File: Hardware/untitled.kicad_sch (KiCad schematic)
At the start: 15 parts, among them IC1 LM74502HDDFR, J3 CarLVPowerConnector, Q12 PSMN8R5-40MSDX

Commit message: revB updates
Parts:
- removed D10: SMBJ30CA, DIOM5436X244N, symbol TVS Diode:SMBJ30CA
- removed D12: CDBC560-G, Schlotty:DIOM7959X262N, symbol Schott:CDBC560-G
- removed LVPRW_TP2: TestPoint, TestPoint:TestPoint_Pad_1.0x1.0mm, symbol Connector:TestPoint
- removed Q12: PSMN8R5-40MSDX, UTSVT_Power:PSMN8R5-40MSDX, symbol utsvt_power:PSMN8R5-40MSDX
- removed R28: 200k, Resistor_SMD:R_0603_1608Metric, symbol Device:R_US
- removed R51: 9.1k, Resistor_SMD:R_0603_1608Metric, symbol Device:R_US
- added C37: 10u, Capacitor_SMD:C_0805_2012Metric_Pad1.18x1.45mm_HandSolder, symbol Device:C
- added C38: 0.1u, Capacitor_SMD:C_0603_1608Metric_Pad1.08x0.95mm_HandSolder, symbol Device:C
- added C5: 1u, Capacitor_SMD:C_0603_1608Metric_Pad1.08x0.95mm_HandSolder, symbol Device:C
- added D10: SMAF4758A, UTSVT_Passives:SODFL5026X125N, symbol Device:D_Zener
- added LVGND_TP1: TestPoint, TestPoint:TestPoint_Pad_2.0x2.0mm, symbol Connector:TestPoint
- added LVPWR1: LED, LED_SMD:LED_0603_1608Metric_Pad1.05x0.95mm_HandSolder, symbol Device:LED
- added Q12, Q2: NVMFWS1D7N04XMT1G, UTSVT_Power:NVMFWS3D0P04M8LT1G, symbol UTSVT_Power:NVMFWS1D7N04XMT1G
- added R14: 200k, Resistor_SMD:R_0603_1608Metric_Pad0.98x0.95mm_HandSolder, symbol Device:R_US
- added R18: 9k, Resistor_SMD:R_0603_1608Metric_Pad0.98x0.95mm_HandSolder, symbol Device:R_US
- added R83: 4.3k, Resistor_SMD:R_0603_1608Metric_Pad0.98x0.95mm_HandSolder, symbol Device:R_US
- 24V_TP1: footprint TestPoint:TestPoint_Pad_1.0x1.0mm -> TestPoint:TestPoint_Pad_2.0x2.0mm
- C20: value 1u -> 220n; footprint Capacitor_SMD:C_0603_1608Metric -> Capacitor_SMD:C_0603_1608Metric_Pad1.08x0.95mm_HandSolder; Manufactuerer TAIYO YUDEN -> (none); Mouser Part Number (none) -> 963-MSASU168SB7224KT; P/N MLASU168SB5105KTNA01 -> MSASU168SB7224KTNB25
- C21: footprint Capacitor_SMD:C_0805_2012Metric -> Capacitor_SMD:C_0805_2012Metric_Pad1.18x1.45mm_HandSolder; Manufactuerer Murata Electronics -> (none); Mouser Part Number (none) -> 81-GRM21BR61H106KE3K
- C3: value 220n -> 1u; footprint Capacitor_SMD:C_0603_1608Metric -> Capacitor_SMD:C_0603_1608Metric_Pad1.08x0.95mm_HandSolder; Manufactuerer TAIYO YUDEN -> (none); Mouser Part Number (none) -> 963-UMK107BJ105KA-T; P/N MSASU168SB7224KTNB25 -> UMK107BJ105KA-T
- C4: Manufactuerer TAIYO YUDEN -> (none); Mouser Part Number (none) -> 963-HMK107B7104KA-T; P/N MLASH168SB7104KTNA01 -> HMK107B7104KA-T
- IC1: Manufactuerer Texas Instruments -> (none); Manufacturer_Part_Number (none) -> LM74502HDDFR
- J3: Manufactuerer Molex -> (none); Mouser Part Number (none) -> 538-105309-1102; P/N 105309-1102 -> 105309-1102
- R28: renamed from R18; footprint Resistor_SMD:R_0603_1608Metric -> Resistor_SMD:R_0603_1608Metric_Pad0.98x0.95mm_HandSolder; Manufactuerer Vishay -> (none); Mouser Part Number (none) -> 71-CRCW060310K0FKEI; P/N CRCW060310K0FKEI -> CRCW060310K0FKEI
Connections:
- net +24V: now also C37.1, C38.1, Q12.5 (D), Q12.6 (D), Q12.7 (D), Q12.8 (D), Q12.9 (D), R83.1; no longer IC1.8 (SRC)
- net GND: now also C3.1, C4.2, C37.2, C38.2, C5.2, D10.2 (A), LVGND_TP1.1, LVPWR1.1 (K), R18.2; no longer C20.1, C4.1
- net LV+: now also C4.1, R28.1, C5.1, Q2.5 (D), Q2.6 (D), Q2.7 (D), Q2.8 (D), Q2.9 (D), R14.1
- net RPP_EN: now also C20.1, C3.2, D10.1 (K); no longer C20.2, C3.1
- net at IC1.4 (VCAP): now also C20.2; no longer C3.2
- net at IC1.6 (GATE): now also Q12.4 (G), Q2.4 (G)
- net at IC1.7 (OV): now also R14.2, R18.1
- new net: IC1.8 (SRC), Q12.1 (S), Q12.2 (S), Q12.3 (S), Q2.1 (S), Q2.2 (S), Q2.3 (S)
- new net: LVPWR1.2 (A), R83.2
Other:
- note added: "24V Input Bypass Cap"
- note added: "LV PWR indicator LED"
- note added: "RPP Protection"
- note removed: "RPP Protection, Direct from VCU (circa 09/09/2025)"
- moved on the sheet: 24V_TP1, 3.3V_In1, IC1, R28

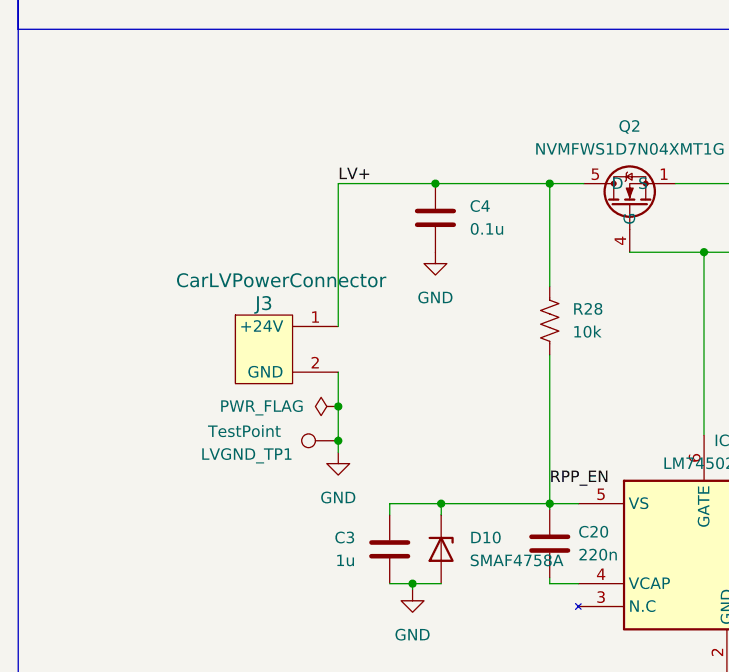
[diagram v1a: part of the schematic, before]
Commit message: Schematic polishes, layout WIP
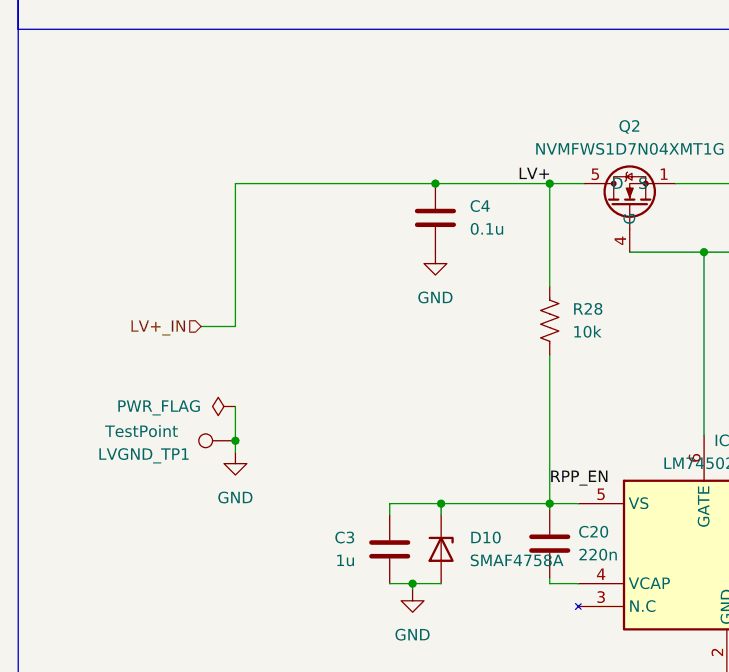
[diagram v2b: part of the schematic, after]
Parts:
- removed J3: CarLVPowerConnector, UTSVT_Connectors:Molex_Nano-Fit_105309-xx02_1x02_P2.50mm_Vertical, symbol UTSVT_Connectors:CarLVPowerConnector
- C20, C3, C38, C4, C5: footprint Capacitor_SMD:C_0603_1608Metric_Pad1.08x0.95mm_HandSolder -> Capacitor_SMD:C_0603_1608Metric
- C21, C37: footprint Capacitor_SMD:C_0805_2012Metric_Pad1.18x1.45mm_HandSolder -> Capacitor_SMD:C_0805_2012Metric
- LVPWR1: footprint LED_SMD:LED_0603_1608Metric_Pad1.05x0.95mm_HandSolder -> LED_SMD:LED_0603_1608Metric
- R14, R18, R28, R83: footprint Resistor_SMD:R_0603_1608Metric_Pad0.98x0.95mm_HandSolder -> Resistor_SMD:R_0603_1608Metric
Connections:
- net LV+ renamed LV+_IN
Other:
- moved on the sheet: LVGND_TP1
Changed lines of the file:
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@@
 	)
 	(junction
-		(at 73.025 53.975)
-		(diameter 0)
-		(color 0 0 0 0)
-	)
-	(junction
 		(at 70.485 98.425)
 		(diameter 0)
@@
 	)
 	(junction
-		(at 62.23 82.55)
+		(at 50.8 82.55)
 		(diameter 0)
 		(color 0 0 0 0)
 	)
 	(junction
-		(at 62.23 78.74)
+		(at 73.025 53.975)
 		(diameter 0)
 		(color 0 0 0 0)
@@
 	(wire
 		(pts
-			(xy 62.23 53.975) (xy 62.23 69.85)
+			(xy 46.99 69.85) (xy 50.8 69.85)
+		)
+		(stroke
+			(width 0)
+			(type default)
+		)
+	)
+	(wire
+		(pts
+			(xy 50.8 53.975) (xy 50.8 69.85)
 		)
 		(stroke
@@
 	(wire
 		(pts
-			(xy 62.23 78.74) (xy 62.23 82.55)
+			(xy 50.8 78.74) (xy 50.8 82.55)
 		)
 		(stroke
@@
 	(wire
 		(pts
-			(xy 62.23 83.82) (xy 62.23 82.55)
+			(xy 50.8 83.82) (xy 50.8 82.55)
 		)
 		(stroke
@@
 	(wire
 		(pts
-			(xy 231.14 69.85) (xy 231.14 78.74)
+			(xy 50.8 53.975) (xy 73.025 53.975)
 		)
 		(stroke
@@
 	(wire
 		(pts
-			(xy 231.14 54.61) (xy 231.14 62.23)
-		)
-		(stroke
-			(width 0)
-			(type default)
-		)
-	)
-	(wire
-		(pts
-			(xy 85.725 89.535) (xy 85.725 90.17)
+			(xy 231.14 69.85) (xy 231.14 78.74)
 		)
 		(stroke
@@
 	(wire
 		(pts
-			(xy 218.44 54.61) (xy 218.44 62.23)
+			(xy 231.14 54.61) (xy 231.14 62.23)
 		)
 		(stroke
@@
 	(wire
 		(pts
-			(xy 140.335 53.975) (xy 140.335 56.515)
+			(xy 85.725 89.535) (xy 85.725 90.17)
 		)
 		(stroke
@@
 	(wire
 		(pts
-			(xy 102.87 61.595) (xy 94.615 61.595)
+			(xy 218.44 54.61) (xy 218.44 62.23)
 		)
 		(stroke
@@
 	(wire
 		(pts
-			(xy 62.23 74.93) (xy 62.23 78.74)
+			(xy 140.335 53.975) (xy 140.335 56.515)
 		)
 		(stroke
@@
 	(wire
 		(pts
-			(xy 62.23 53.975) (xy 73.025 53.975)
+			(xy 102.87 61.595) (xy 94.615 61.595)
 		)
 		(stroke
@@
 		)
 	)
-	(label "LV+"
-		(at 62.23 53.975 0)
+	(label "RPP_EN"
+		(at 85.725 87.63 0)
 		(effects
 			(font
@@
 		)
 	)
-	(label "RPP_EN"
-		(at 85.725 87.63 0)
+	(label "LV+"
+		(at 241.3 54.61 0)
 		(effects
 			(font
@@
 	)
 	(label "LV+"
-		(at 241.3 54.61 0)
+		(at 125.73 79.375 0)
 		(effects
 			(font
@@
 	)
 	(label "LV+"
-		(at 125.73 79.375 0)
+		(at 82.2147 53.975 0)
 		(effects
 			(font
@@
 		)
 	)
+	(hierarchical_label "LV+_IN"
+		(shape input)
+		(at 46.99 69.85 180)
+		(effects
+			(font
+				(size 1.27 1.27)
+			)
+			(justify right)
+		)
+	)
 	(symbol
 		(lib_id "Device:C")
@@
 			)
 		)
-		(property "Footprint" "Capacitor_SMD:C_0603_1608Metric_Pad1.08x0.95mm_HandSolder"
+		(property "Footprint" "Capacitor_SMD:C_0603_1608Metric"
 			(at 242.2652 69.85 0)
 			(effects
@@
 			)
 		)
-		(property "Footprint" "Resistor_SMD:R_0603_1608Metric_Pad0.98x0.95mm_HandSolder"
+		(property "Footprint" "Resistor_SMD:R_0603_1608Metric"
 			(at 126.746 86.614 90)
 			(effects
@@
 			)
 		)
-		(property "Footprint" "Capacitor_SMD:C_0603_1608Metric_Pad1.08x0.95mm_HandSolder"
+		(property "Footprint" "Capacitor_SMD:C_0603_1608Metric"
 			(at 84.7598 97.79 0)
 			(effects
@@
 			)
 		)
-		(property "Footprint" "Resistor_SMD:R_0603_1608Metric_Pad0.98x0.95mm_HandSolder"
+		(property "Footprint" "Resistor_SMD:R_0603_1608Metric"
 			(at 86.741 69.469 90)
 			(effects
@@
 			)
 		)
-		(property "Footprint" "Capacitor_SMD:C_0603_1608Metric_Pad1.08x0.95mm_HandSolder"
+		(property "Footprint" "Capacitor_SMD:C_0603_1608Metric"
 			(at 68.9102 90.805 0)
 			(effects
@@
 			)
 		)
-		(property "Footprint" "Resistor_SMD:R_0603_1608Metric_Pad0.98x0.95mm_HandSolder"
+		(property "Footprint" "Resistor_SMD:R_0603_1608Metric"
 			(at 135.509 92.329 90)
 			(effects
@@
 	(symbol
 		(lib_id "Connector:TestPoint")
-		(at 62.23 82.55 90)
+		(at 50.8 82.55 90)
 		(unit 1)
 		(exclude_from_sim no)
@@
 		(dnp no)
 		(property "Reference" "LVGND_TP1"
-			(at 52.07 84.074 90)
+			(at 40.64 84.074 90)
 			(effects
 				(font
@@
 		)
 		(property "Value" "TestPoint"
-			(at 51.816 81.534 90)
+			(at 40.386 81.534 90)
 			(effects
 				(font
@@
 		)
 		(property "Footprint" "TestPoint:TestPoint_Pad_2.0x2.0mm"
-			(at 62.23 77.47 0)
+			(at 50.8 77.47 0)
 			(effects
 				(font
@@
 		)
 		(property "Datasheet" "~"
-			(at 62.23 77.47 0)
+			(at 50.8 77.47 0)
 			(effects
 				(font
@@
 		)
 		(property "Description" "test point"
-			(at 62.23 82.55 0)
+			(at 50.8 82.55 0)
 			(effects
 				(font
@@
 			)
 		)
-		(property "Footprint" "Capacitor_SMD:C_0805_2012Metric_Pad1.18x1.45mm_HandSolder"
+		(property "Footprint" "Capacitor_SMD:C_0805_2012Metric"
 			(at 219.4052 69.85 0)
 			(effects
@@
 	)
 	(symbol
-		(lib_id "UTSVT_Connectors:CarLVPowerConnector")
-		(at 54.61 72.39 0)
-		(unit 1)
-		(exclude_from_sim no)
-		(in_bom yes)
-		(on_board yes)
-		(dnp no)
-		(property "Reference" "J3"
-			(at 53.975 67.31 0)
-			(effects
-				(font
-					(size 1.524 1.524)
-				)
-			)
-		)
-		(property "Value" "CarLVPowerConnector"
-			(at 55.88 64.77 0)
-			(effects
-				(font
-					(size 1.524 1.524)
-				)
-			)
-		)
-		(property "Footprint" "UTSVT_Connectors:Molex_Nano-Fit_105309-xx02_1x02_P2.50mm_Vertical"
-			(at 54.61 72.39 0)
-			(effects
-				(font
-					(size 1.524 1.524)
-				)
-				(hide yes)
-			)
-		)
-		(property "Datasheet" ""
-			(at 54.61 72.39 0)
-			(effects
-				(font
-					(size 1.524 1.524)
-				)
-				(hide yes)
-			)
-		)
-		(property "Description" "Connector for the car's 24V power bus"
-			(at 54.61 72.39 0)
-			(effects
-				(font
-					(size 1.27 1.27)
-				)
-				(hide yes)
-			)
-		)
-		(property "P/N" "105309-1102"
-			(at 54.61 72.39 0)
-			(effects
-				(font
-					(size 1.27 1.27)
-				)
-				(hide yes)
-			)
-		)
-		(property "Mouser Part Number" " 538-105309-1102"
-			(at 54.61 72.39 0)
-			(effects
-				(font
-					(size 1.27 1.27)
-				)
-				(hide yes)
-			)
-		)
-		(pin "1"
-		)
-		(pin "2"
-		)
-		(instances
-			(project "BPS-Leader"
-				(path "/fb37da34-e420-4994-8cc1-079e8c0fa48e/a39d8cf5-dc9c-4f60-80f8-399517c69b53"
-					(reference "J3")
-					(unit 1)
-				)
-			)
-		)
-	)
-	(symbol
 		(lib_id "UTSVT_ICs:LM74502HDDFR")
 		(at 88.9 89.535 0)
@@
 			)
 		)
-		(property "Footprint" "Capacitor_SMD:C_0603_1608Metric_Pad1.08x0.95mm_HandSolder"
+		(property "Footprint" "Capacitor_SMD:C_0603_1608Metric"
 			(at 73.9902 61.595 0)
 			(effects
@@
 			)
 		)
-		(property "Footprint" "Capacitor_SMD:C_0805_2012Metric_Pad1.18x1.45mm_HandSolder"
+		(property "Footprint" "Capacitor_SMD:C_0805_2012Metric"
 			(at 141.3002 64.135 0)
 			(effects
@@
 			)
 		)
-		(property "Footprint" "Capacitor_SMD:C_0603_1608Metric_Pad1.08x0.95mm_HandSolder"
+		(property "Footprint" "Capacitor_SMD:C_0603_1608Metric"
 			(at 232.1052 69.85 0)
 			(effects
@@
 	(symbol
 		(lib_id "power:PWR_FLAG")
-		(at 62.23 78.74 90)
+		(at 50.8 78.74 90)
 		(unit 1)
 		(exclude_from_sim no)
@@
 		(fields_autoplaced yes)
 		(property "Reference" "#FLG02"
-			(at 60.325 78.74 0)
+			(at 48.895 78.74 0)
 			(effects
 				(font
@@
 		)
 		(property "Value" "PWR_FLAG"
-			(at 58.42 78.7399 90)
+			(at 46.99 78.7399 90)
 			(effects
 				(font
@@
 		)
 		(property "Footprint" ""
-			(at 62.23 78.74 0)
+			(at 50.8 78.74 0)
 			(effects
 				(font
@@
 		)
 		(property "Datasheet" "~"
-			(at 62.23 78.74 0)
+			(at 50.8 78.74 0)
 			(effects
 				(font
@@
 		)
 		(property "Description" "Special symbol for telling ERC where power comes from"
-			(at 62.23 78.74 0)
+			(at 50.8 78.74 0)
 			(effects
 				(font
@@
 	(symbol
 		(lib_id "power:GND")
-		(at 62.23 83.82 0)
+		(at 50.8 83.82 0)
 		(unit 1)
 		(exclude_from_sim no)
@@
 		(fields_autoplaced yes)
 		(property "Reference" "#PWR030"
-			(at 62.23 90.17 0)
+			(at 50.8 90.17 0)
 			(effects
 				(font
@@
 		)
 		(property "Value" "GND"
-			(at 62.23 88.9 0)
+			(at 50.8 88.9 0)
 			(effects
 				(font
@@
 		)
 		(property "Footprint" ""
-			(at 62.23 83.82 0)
+			(at 50.8 83.82 0)
 			(effects
 				(font
@@
 		)
 		(property "Datasheet" ""
-			(at 62.23 83.82 0)
+			(at 50.8 83.82 0)
 			(effects
 				(font
@@
 		)
 		(property "Description" "Power symbol creates a global label with name \"GND\" , ground"
-			(at 62.23 83.82 0)
+			(at 50.8 83.82 0)
 			(effects
 				(font
@@
 			)
 		)
-		(property "Footprint" "LED_SMD:LED_0603_1608Metric_Pad1.05x0.95mm_HandSolder"
+		(property "Footprint" "LED_SMD:LED_0603_1608Metric"
 			(at 203.2 69.85 0)
 			(effects
@@
 			)
 		)
-		(property "Footprint" "Resistor_SMD:R_0603_1608Metric_Pad0.98x0.95mm_HandSolder"
+		(property "Footprint" "Resistor_SMD:R_0603_1608Metric"
 			(at 204.216 61.214 90)
 			(effects

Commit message: circuit blocks designed, schematic updated
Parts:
- removed 24V_TP1, LVGND_TP1: TestPoint, TestPoint:TestPoint_Pad_2.0x2.0mm, symbol Connector:TestPoint
- removed 3.3V_In1: Conn_01x02, UTSVT_Connectors:Molex_Nano-Fit_105309-xx02_1x02_P2.50mm_Vertical, symbol Connector_Generic:Conn_01x02
- renumbered Q2 to Q13
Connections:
- net +24V renamed LV_OUT
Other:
- note removed: "3.3V injector"

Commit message: JLC Production Files
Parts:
- C20: LCSC (none) -> C344195
- C21, C37: LCSC (none) -> C440198
- C3, C5: LCSC (none) -> C15849
- C38, C4: LCSC (none) -> C14663
- D10: footprint UTSVT_Passives:SODFL5026X125N -> UTSVT_Passives:SODFL4724X108N; LCSC (none) -> C183490
- IC1: LCSC (none) -> C5219202
- LVPWR1: LCSC (none) -> C7371904
- Q12, Q13: LCSC (none) -> C133142
- R14: LCSC (none) -> C25811
- R18: LCSC (none) -> C3016444
- R28: LCSC (none) -> C25804
- R83: LCSC (none) -> C2907165
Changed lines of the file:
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@@
+			)
+		)
+		(property "LCSC" "C15849"
+			(at 245.11 64.7699 0)
+			(effects
+				(font
+					(size 1.27 1.27)
+				)
+				(hide yes)
 			)
 		)
@@
 			)
 		)
+		(property "LCSC" "C25811"
+			(at 127.635 85.0899 0)
+			(effects
+				(font
+					(size 1.27 1.27)
+				)
+				(hide yes)
+			)
+		)
 		(pin "1"
 		)
@@
 		(on_board yes)
 		(dnp no)
-		(fields_autoplaced yes)
 		(property "Reference" "D10"
 			(at 76.835 93.3449 90)
@@
 		)
 		(property "Value" "SMAF4758A"
-			(at 76.835 95.8849 90)
+			(at 73.914 97.79 90)
 			(effects
 				(font
@@
 			)
 		)
-		(property "Footprint" "UTSVT_Passives:SODFL5026X125N"
+		(property "Footprint" "UTSVT_Passives:SODFL4724X108N"
 			(at 73.66 94.615 0)
 			(effects
@@
 		(property "Description" "Zener diode"
 			(at 73.66 94.615 0)
+			(effects
+				(font
+					(size 1.27 1.27)
+				)
+				(hide yes)
+			)
+		)
+		(property "LCSC" "C183490"
+			(at 76.835 93.3449 0)
 			(effects
 				(font
@@
 			)
 		)
+		(property "LCSC" "C344195"
+			(at 88.9 92.7099 0)
+			(effects
+				(font
+					(size 1.27 1.27)
+				)
+				(hide yes)
+			)
+		)
 		(pin "2"
 		)
@@
 			)
 		)
+		(property "LCSC" "C25804"
+			(at 88.265 67.9449 0)
+			(effects
+				(font
+					(size 1.27 1.27)
+				)
+				(hide yes)
+			)
+		)
 		(pin "1"
 		)
@@
 			)
 		)
+		(property "LCSC" "C15849"
+			(at 64.135 93.3449 0)
+			(effects
+				(font
+					(size 1.27 1.27)
+				)
+				(hide yes)
+			)
+		)
 		(pin "2"
 		)
@@
 			)
 		)
+		(property "LCSC" "C133142"
+			(at 120.65 47.625 0)
+			(effects
+				(font
+					(size 1.27 1.27)
+				)
+				(hide yes)
+			)
+		)
 		(pin "8"
 		)
@@
 			)
 		)
+		(property "LCSC" "C3016444"
+			(at 135.255 86.995 0)
+			(effects
+				(font
+					(size 1.27 1.27)
+				)
+				(hide yes)
+			)
+		)
 		(pin "1"
 		)
@@
 			)
 		)
+		(property "LCSC" "C440198"
+			(at 222.25 64.7699 0)
+			(effects
+				(font
+					(size 1.27 1.27)
+				)
+				(hide yes)
+			)
+		)
 		(pin "1"
 		)
@@
 			)
 		)
+		(property "LCSC" "C5219202"
+			(at 105.41 82.55 0)
+			(effects
+				(font
+					(size 1.27 1.27)
+				)
+				(hide yes)
+			)
+		)
 		(pin "1"
 		)
@@
 			)
 		)
+		(property "LCSC" "C14663"
+			(at 76.835 56.5149 0)
+			(effects
+				(font
+					(size 1.27 1.27)
+				)
+				(hide yes)
+			)
+		)
 		(pin "1"
 		)
@@
 		(property "Mouser Part Number" "81-GRM21BR61H106KE3K"
 			(at 140.335 60.325 0)
+			(effects
+				(font
+					(size 1.27 1.27)
+				)
+				(hide yes)
+			)
+		)
+		(property "LCSC" "C440198"
+			(at 143.51 59.0549 0)
 			(effects
 				(font
@@
 			)
 		)
+		(property "LCSC" "C14663"
+			(at 234.315 64.7699 0)
+			(effects
+				(font
+					(size 1.27 1.27)
+				)
+				(hide yes)
+			)
+		)
 		(pin "1"
 		)
@@
 			)
 		)
+		(property "LCSC" "C133142"
+			(at 94.615 46.99 0)
+			(effects
+				(font
+					(size 1.27 1.27)
+				)
+				(hide yes)
+			)
+		)
 		(pin "8"
 		)
@@
 		(property "P/N" "XL-1608UBC-06A"
 			(at 203.2 69.85 0)
+			(effects
+				(font
+					(size 1.27 1.27)
+				)
+				(hide yes)
+			)
+		)
+		(property "LCSC" "C7371904"
+			(at 207.518 69.85 0)
 			(effects
 				(font
@@
 			(effects
 				(font
+					(size 1.27 1.27)
+				)
+				(hide yes)
+			)
+		)
+		(property "LCSC" "C2907165"
+			(at 205.74 59.6899 0)
+			(effects
+				(font
